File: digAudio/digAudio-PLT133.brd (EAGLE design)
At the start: 18.8 x 19.7 mm, 12 parts, among them IC1 DIT4096-H

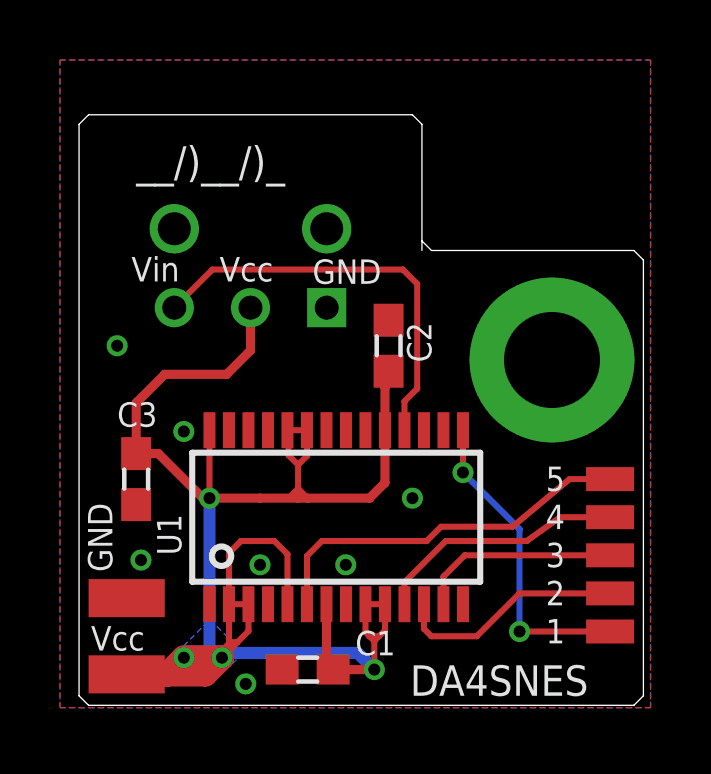
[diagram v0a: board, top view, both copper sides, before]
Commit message: bugfix on PCBs: - pin 14 (M/nS) was floating - now it is properly connected to GND
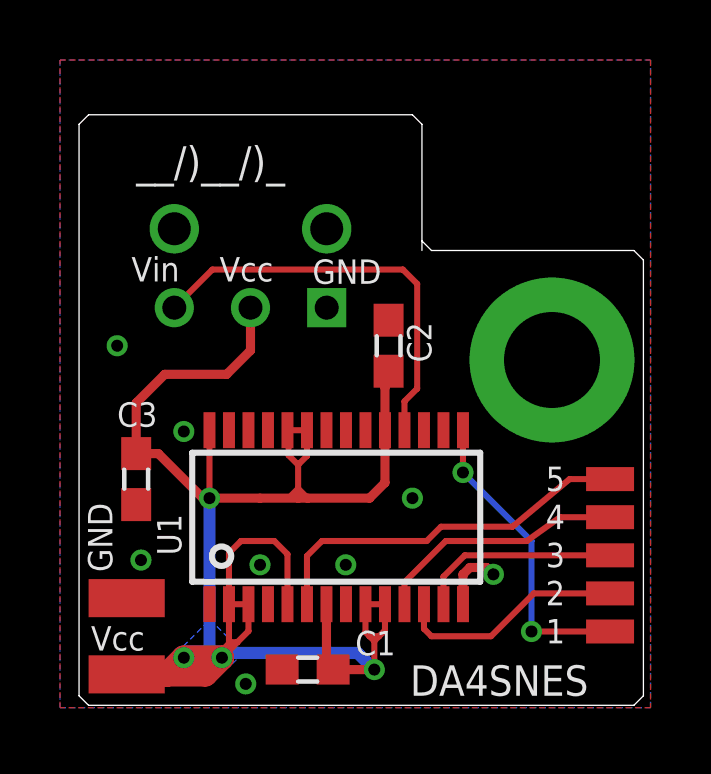
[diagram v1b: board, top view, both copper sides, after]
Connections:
- net GND: now also IC1.14
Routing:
- net GND: track 0.00 -> 2.20 mm, vias 8 -> 9
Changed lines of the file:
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@@
 <?xml version="1.0" encoding="utf-8"?>
 <!DOCTYPE eagle SYSTEM "eagle.dtd">
-<eagle version="8.6.0">
+<eagle version="9.6.2">
 <drawing>
 <settings>
@@
 <param name="checkStop" value="0"/>
 <param name="checkValues" value="0"/>
+<param name="checkNames" value="1"/>
+<param name="checkWireStubs" value="1"/>
+<param name="checkPolygonWidth" value="0"/>
 <param name="useDiameter" value="13"/>
 <param name="maxErrors" value="50"/>
@@
 <element name="3" library="wirepad" package="SMD0,8-1,6" value="" x="18.335625" y="5.08" smashed="yes" rot="R90"/>
 <element name="1" library="wirepad" package="SMD0,8-1,6" value="" x="18.335625" y="2.54" smashed="yes" rot="R90"/>
-<element name="U$1" library="cs8406" package="PLT133/T10W" value="PLT133/T10W" x="6.35" y="13.335" rot="MR0"/>
+<element name="U$1" library="cs8406" package="PLT133/T10W" value="PLT133/T10W" x="6.35" y="13.335" smashed="yes" rot="MR0"/>
 </elements>
 <signals>
@@
 <via x="6.19125" y="0.79375" extent="1-16" drill="0.4"/>
 <contactref element="U$1" pad="P$1"/>
+<contactref element="IC1" pad="14"/>
+<via x="14.44625" y="4.445" extent="1-16" drill="0.4"/>
+<wire x1="13.4325" y1="3.45" x2="13.4325" y2="4.4440125" width="0.3048" layer="1"/>
+<wire x1="13.4325" y1="4.4440125" x2="13.66205625" y2="4.67356875" width="0.3048" layer="1"/>
+<wire x1="13.66205625" y1="4.67356875" x2="14.21768125" y2="4.67356875" width="0.3048" layer="1"/>
+<wire x1="14.21768125" y1="4.67356875" x2="14.44625" y2="4.445" width="0.3048" layer="1"/>
 </signal>
 <signal name="VCC">
@@
 <contactref element="IC1" pad="15"/>
 <contactref element="1" pad="P$1"/>
-<wire x1="18.335625" y1="2.54" x2="15.319375" y2="2.54" width="0.2032" layer="1"/>
-<via x="15.319375" y="2.54" extent="1-16" drill="0.4"/>
-<wire x1="15.319375" y1="2.54" x2="15.319375" y2="5.953125" width="0.2032" layer="16"/>
-<wire x1="15.319375" y1="5.953125" x2="13.4325" y2="7.84" width="0.2032" layer="16"/>
+<wire x1="18.335625" y1="2.54" x2="15.71625" y2="2.54" width="0.2032" layer="1"/>
+<via x="15.71625" y="2.54" extent="1-16" drill="0.4"/>
+<wire x1="15.71625" y1="2.54" x2="15.71625" y2="5.55625" width="0.2032" layer="16"/>
+<wire x1="15.71625" y1="5.55625" x2="13.4325" y2="7.84" width="0.2032" layer="16"/>
 <via x="13.4325" y="7.84" extent="1-16" drill="0.4"/>
 <wire x1="13.4325" y1="9.25" x2="13.4325" y2="7.84" width="0.2032" layer="1"/>
@@
 <wire x1="12.1325" y1="3.45" x2="12.1325" y2="2.63125" width="0.2032" layer="1"/>
 <wire x1="12.1325" y1="2.63125" x2="12.3825" y2="2.38125" width="0.2032" layer="1"/>
-<wire x1="12.3825" y1="2.38125" x2="13.890625" y2="2.38125" width="0.2032" layer="1"/>
-<wire x1="13.890625" y1="2.38125" x2="15.319375" y2="3.81" width="0.2032" layer="1"/>
-<wire x1="15.319375" y1="3.81" x2="18.335625" y2="3.81" width="0.2032" layer="1"/>
+<wire x1="12.3825" y1="2.38125" x2="14.366875" y2="2.38125" width="0.2032" layer="1"/>
+<wire x1="14.366875" y1="2.38125" x2="15.795625" y2="3.81" width="0.2032" layer="1"/>
+<wire x1="15.795625" y1="3.81" x2="18.335625" y2="3.81" width="0.2032" layer="1"/>
 </signal>
 <signal name="N$6">
@@
 </signal>
 </signals>
+<mfgpreviewcolors>
+<mfgpreviewcolor name="soldermaskcolor" color="0xC8008000"/>
+<mfgpreviewcolor name="silkscreencolor" color="0xFFFEFEFE"/>
+<mfgpreviewcolor name="backgroundcolor" color="0xFF282828"/>
+<mfgpreviewcolor name="coppercolor" color="0xFFFFBF00"/>
+<mfgpreviewcolor name="substratecolor" color="0xFF786E46"/>
+</mfgpreviewcolors>
 </board>
 </drawing>
